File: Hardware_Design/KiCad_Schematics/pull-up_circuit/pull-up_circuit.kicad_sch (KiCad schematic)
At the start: 6 parts, among them J2 Conn_01x01_Pin, J3 Conn_01x01_Pin, SW2 SW_Push

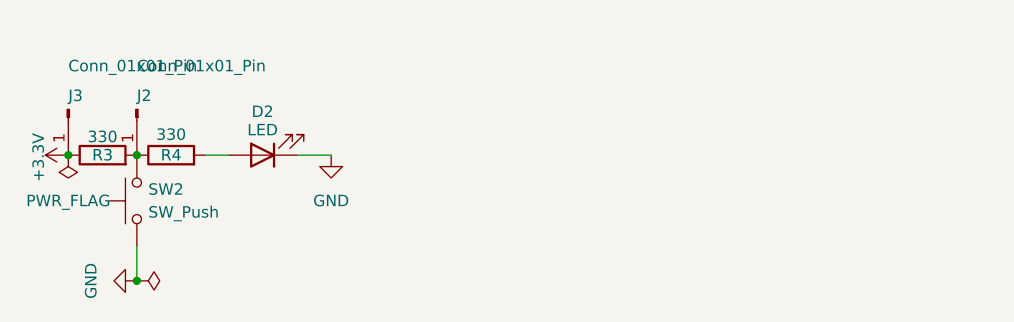
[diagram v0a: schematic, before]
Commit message: Add README.md and update pull-up circuit schematic
Added the README.md file and made minor adjustments to the pull-up circuit schematic to fix small bugs/issues.
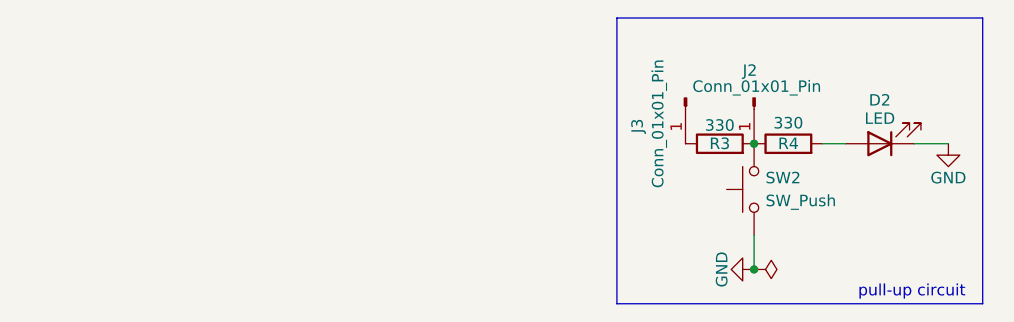
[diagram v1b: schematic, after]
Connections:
- net +3.3V: no longer names the net of J3.1 (Pin_1), R3.1
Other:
- note added: "pull-up circuit"
- moved on the sheet: D2, J2, J3, R3, R4, SW2
